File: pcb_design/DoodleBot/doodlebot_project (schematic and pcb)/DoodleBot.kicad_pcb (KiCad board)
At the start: 2 copper layers, 82.9 x 56.1 mm, 45 parts, among them J1 Conn_01x04, J2 Conn_01x04, J3 USB_B_Micro, J4 BUZZER_HEADERS, J5 LED_HEADERS, J6 MARKER_HEADERS, J7 ERASER_HEADERS, U1 ESP32-S3-WROOM-1

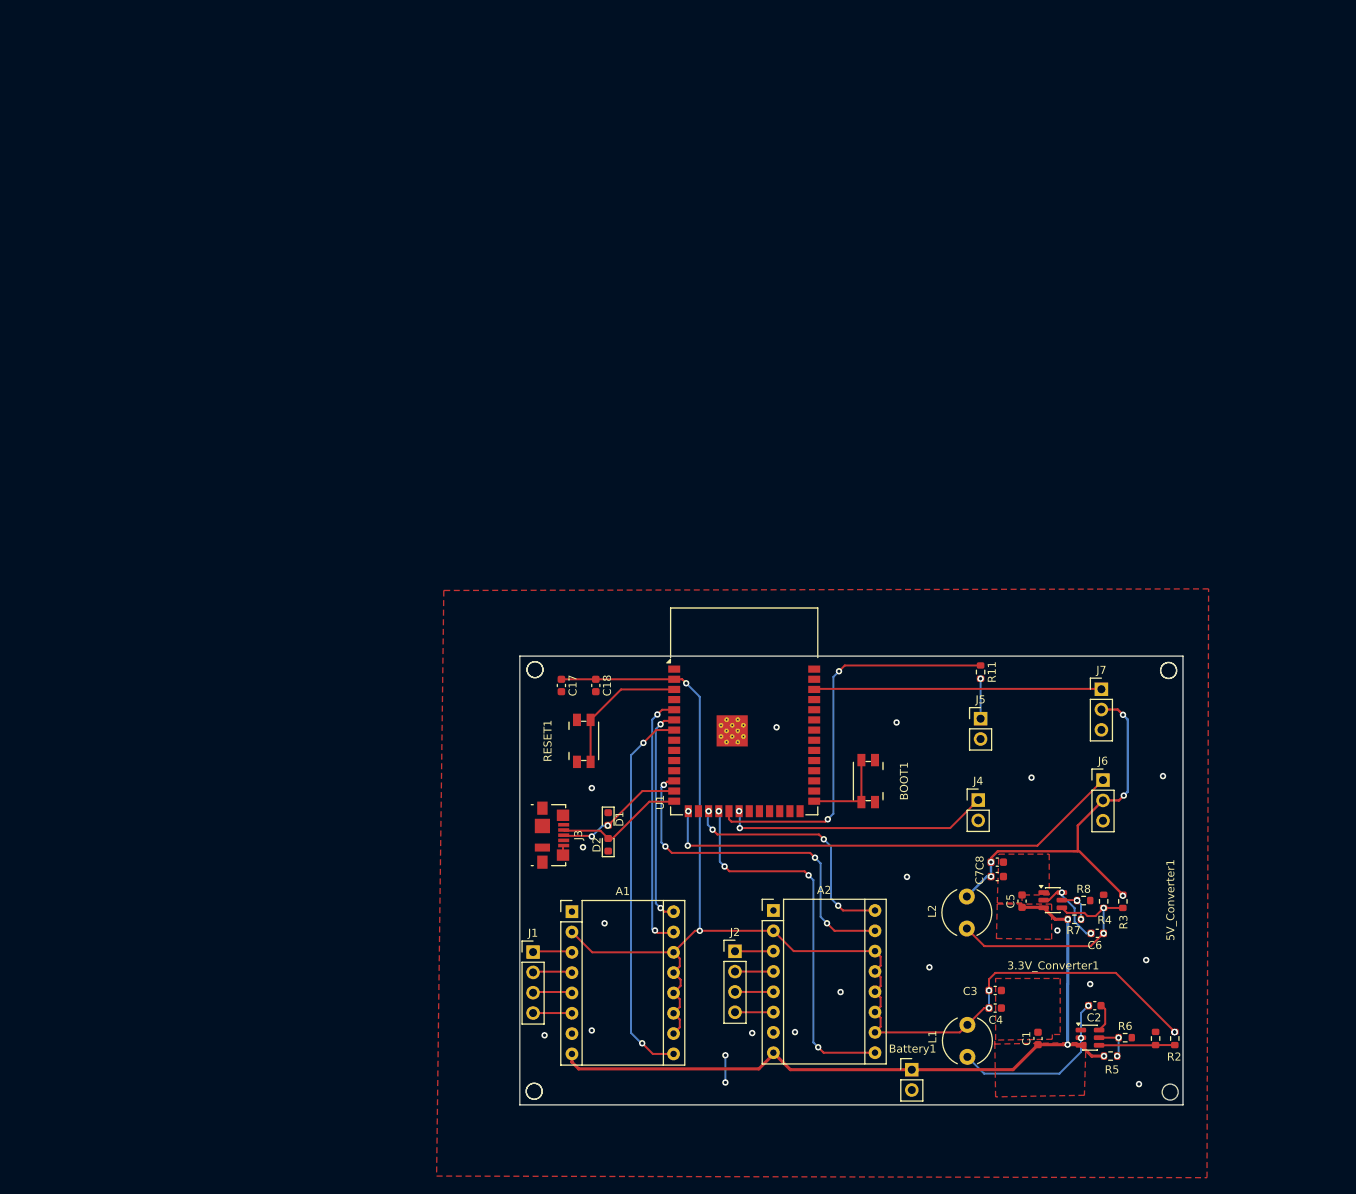
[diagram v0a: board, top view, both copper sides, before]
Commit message: Reorganized project structure
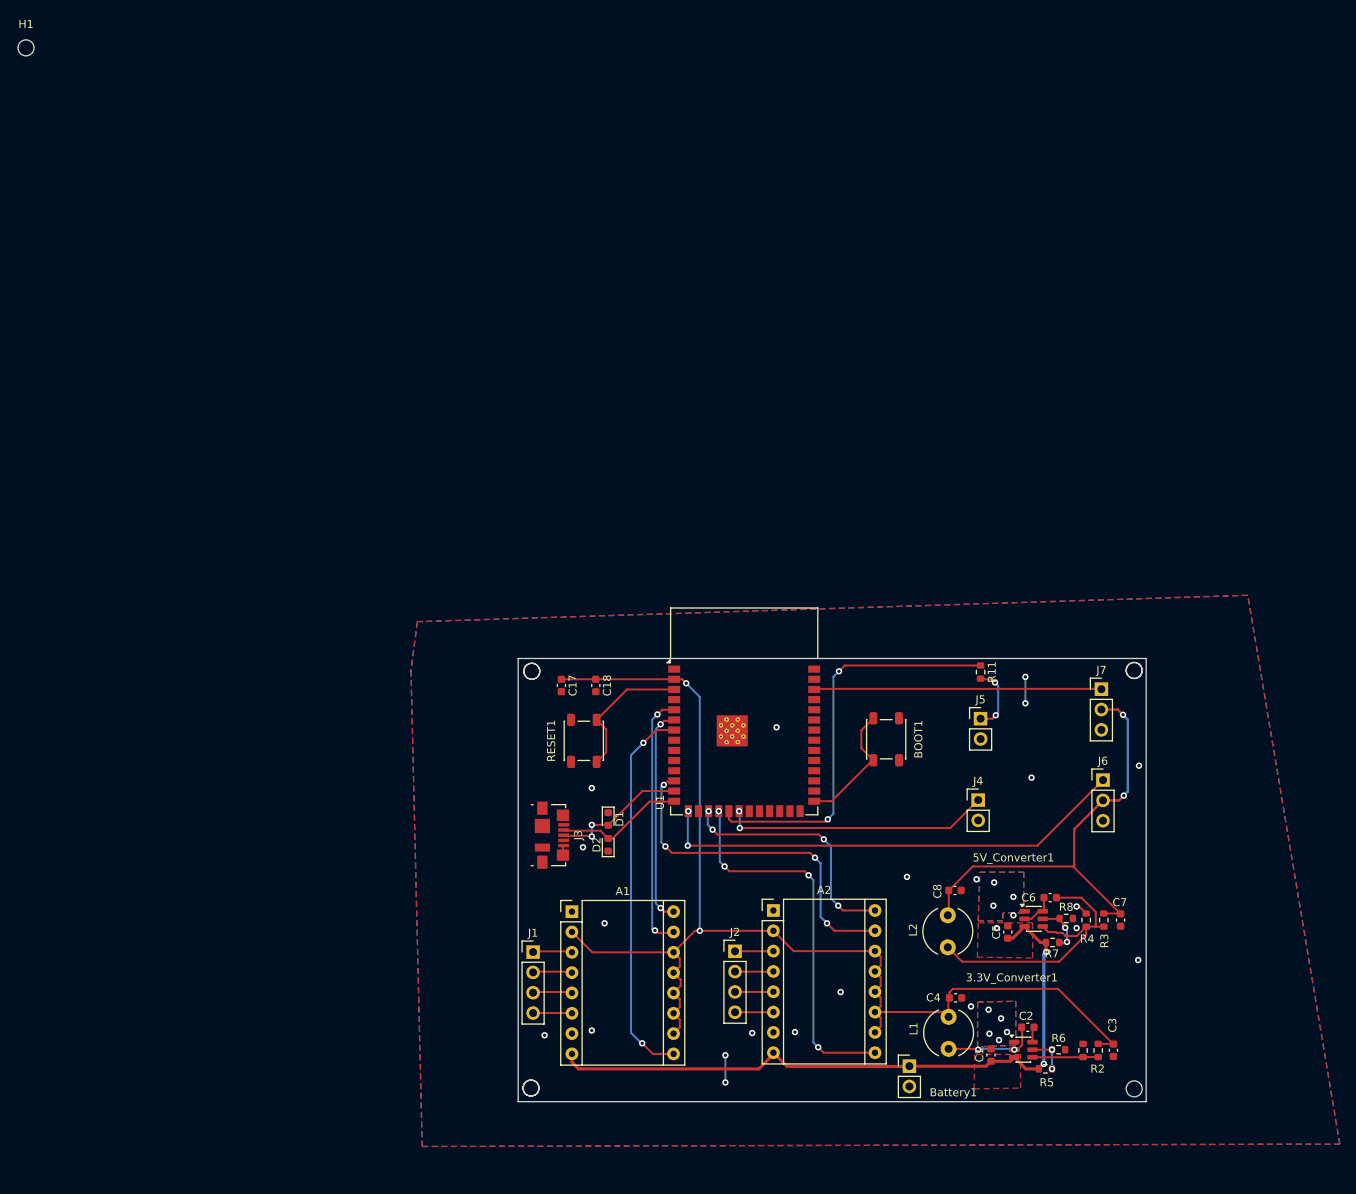
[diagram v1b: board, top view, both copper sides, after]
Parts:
- added H1: MountingHole, MountingHole:MountingHole_2mm, F.Cu at (2.27, 2.27)
- BOOT1, RESET1: footprint Button_Switch_SMD:Panasonic_EVQPUJ_EVQPUA -> Button_Switch_SMD:SW_SPST_PTS647_Sx38
- moved C3 16.6 mm to (138.2, 127.6), turned to 90 degrees
- moved C7 16.4 mm to (139.1, 111.3), turned to 90 degrees
- moved R2 9.69 mm to (136.3, 127.6)
- moved R1 9.20 mm to (134.4, 127.6)
- moved C2 8.80 mm to (127.5, 124.7)
- moved R6 8.46 mm to (131.3, 127.5)
- moved 3.3V_Converter1 8.46 mm to (127.0, 127.5)
- moved R5 8.31 mm to (129.7, 129.9)
- moved C6 7.38 mm to (130.3, 108.5)
- moved C8 6.36 mm to (118.4, 107.6)
- moved C1 6.23 mm to (122.9, 128.2)
- moved BOOT1 5.69 mm to (109.8, 88.7)
- moved C4 5.11 mm to (118.5, 121.0)
- moved ? 4.52 mm to (140.8, 132.4)
- moved ? 4.30 mm to (140.8, 80.1)
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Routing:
- net Net-(3.3V_Converter1-SW): track 22.4 -> 11.8 mm
- net +12V: track 93.8 -> 84.9 mm, vias 3 -> 2
- net +3V3: track 159.6 -> 152.0 mm, vias 6 -> 2
- net +5V: track 50.4 -> 56.7 mm, vias 5 -> 2
- net Net-(5V_Converter1-FB): track 30.5 -> 36.8 mm, vias 2 -> 0
- net Net-(5V_Converter1-BOOT): track 9.72 -> 4.52 mm, vias 2 -> 0
- net GND: track 5.01 -> 9.87 mm, vias 20 -> 31
- net Net-(U1-IO0): track 11.2 -> 16.0 mm
- net Net-(J5-Pin_1): track 5.00 -> 8.46 mm, vias 1 -> 2
- net Net-(5V_Converter1-EN): track 4.57 -> 6.97 mm, vias 3 -> 2
- net Net-(3.3V_Converter1-BOOT): track 3.64 -> 1.93 mm
- net Net-(3.3V_Converter1-FB): track 9.53 -> 8.22 mm
- net Net-(D1-A2): track 16.2 -> 17.1 mm
- added copper zone on B.Cu, net GND
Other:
- board size 82.9 x 56.1 mm -> 78.5 x 55.4 mm

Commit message: Added wider 12V traces from 0.39mm to 0.45mm
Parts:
- removed H1: MountingHole, MountingHole:MountingHole_2mm
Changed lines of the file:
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@@
 			(drillshape 0)
 			(scaleselection 1)
-			(outputdirectory "./")
+			(outputdirectory "doodlebot_gerber/")
 		)
 	)
@@
 		(embedded_fonts no)
 	)
-	(footprint "MountingHole:MountingHole_2mm"
-		(layer "F.Cu")
-		(at 2.275 2.275)
-		(descr "Mounting Hole 2mm, no annular, generated by kicad-footprint-generator mountinghole.py")
-		(tags "mountinghole")
-		(property "Reference" "H1"
-			(at 0 -2.95 0)
-			(layer "F.SilkS")
-			(effects
-				(font
-					(size 1 1)
-					(thickness 0.15)
-				)
-			)
-		)
-		(property "Value" "MountingHole"
-			(at 0 2.95 0)
-			(layer "F.Fab")
-			(effects
-				(font
-					(size 1 1)
-					(thickness 0.15)
-				)
-			)
-		)
-		(property "Datasheet" "~"
-			(at 0 0 0)
-			(layer "F.Fab")
-			(hide yes)
-			(effects
-				(font
-					(size 1.27 1.27)
-					(thickness 0.15)
-				)
-			)
-		)
-		(property "Description" "Mounting Hole without connection"
-			(at 0 0 0)
-			(layer "F.Fab")
-			(hide yes)
-			(effects
-				(font
-					(size 1.27 1.27)
-					(thickness 0.15)
-				)
-			)
-		)
-		(property ki_fp_filters "MountingHole*")
-		(sheetname "/")
-		(sheetfile "DoodleBot.kicad_sch")
-		(attr exclude_from_pos_files exclude_from_bom)
-		(fp_circle
-			(center 0 0)
-			(end 2 0)
-			(stroke
-				(width 0.15)
-				(type solid)
-			)
-			(fill no)
-			(layer "Cmts.User")
-		)
-		(fp_circle
-			(center 0 0)
-			(end 2.25 0)
-			(stroke
-				(width 0.05)
-				(type solid)
-			)
-			(fill no)
-			(layer "F.CrtYd")
-		)
-		(fp_text user "${REFERENCE}"
-			(at 0 0 0)
-			(layer "F.Fab")
-			(effects
-				(font
-					(size 1 1)
-					(thickness 0.15)
-				)
-			)
-		)
-		(pad "" np_thru_hole circle
-			(at 0 0)
-			(size 2 2)
-			(drill 2)
-			(layers "*.Cu" "*.Mask")
-		)
-		(embedded_fonts no)
-	)
 	(footprint ""
 		(layer "F.Cu")
@@
 		(start 125.3125 128.95)
 		(end 125.8125 128.45)
-		(width 0.39)
+		(width 0.45)
 		(layer "F.Cu")
 		(net 5)
@@
 		(start 127.2625 129.9)
 		(end 125.8125 128.45)
-		(width 0.39)
+		(width 0.45)
 		(layer "F.Cu")
 		(net 5)
@@
 		(start 128.875 129.9)
 		(end 127.2625 129.9)
-		(width 0.39)
+		(width 0.45)
 		(layer "F.Cu")
 		(net 5)
@@
 	)
 	(segment
-		(start 95.7 128.08)
-		(end 93.88 129.9)
-		(width 0.39)
-		(layer "F.Cu")
-		(net 5)
-	)
-	(segment
 		(start 129.775 114.1)
 		(end 129.775 115.275)
-		(width 0.39)
+		(width 0.45)
 		(layer "F.Cu")
 		(net 5)
 	)
 	(segment
-		(start 93.88 129.9)
-		(end 71.36 129.9)
+		(start 112.66 129.6)
+		(end 112.7 129.56)
 		(width 0.39)
 		(layer "F.Cu")
@@
 	)
 	(segment
-		(start 112.66 129.6)
-		(end 112.7 129.56)
-		(width 0.39)
+		(start 71.06 129.6)
+		(end 70.52 129.06)
+		(width 0.45)
 		(layer "F.Cu")
 		(net 5)
@@
 		(start 122.9 128.95)
 		(end 125.3125 128.95)
-		(width 0.39)
+		(width 0.45)
 		(layer "F.Cu")
 		(net 5)
@@
 		(start 112.7 129.56)
 		(end 122.29 129.56)
-		(width 0.39)
+		(width 0.45)
 		(layer "F.Cu")
 		(net 5)
@@
 		(start 129.5 129.275)
 		(end 128.875 129.9)
-		(width 0.39)
+		(width 0.45)
 		(layer "F.Cu")
 		(net 5)
@@
 		(start 97.42 129.6)
 		(end 112.66 129.6)
-		(width 0.39)
+		(width 0.45)
 		(layer "F.Cu")
 		(net 5)
@@
 	)
 	(segment
-		(start 70.52 129.06)
-		(end 70.52 128.03)
-		(width 0.39)
-		(layer "F.Cu")
-		(net 5)
-	)
-	(segment
 		(start 125.8125 128.45)
 		(end 125.75 128.45)
@@
 		(start 129.1 114.1)
 		(end 127.1 112.1)
-		(width 0.39)
+		(width 0.45)
+		(layer "F.Cu")
+		(net 5)
+	)
+	(segment
+		(start 95.7 128.08)
+		(end 94.18 129.6)
+		(width 0.45)
 		(layer "F.Cu")
 		(net 5)
@@
 		(start 95.7 127.88)
 		(end 97.42 129.6)
-		(width 0.39)
+		(width 0.45)
+		(layer "F.Cu")
+		(net 5)
+	)
+	(segment
+		(start 70.52 129.06)
+		(end 70.52 128.03)
+		(width 0.45)
 		(layer "F.Cu")
 		(net 5)
@@
 		(start 129.775 114.1)
 		(end 129.1 114.1)
-		(width 0.39)
+		(width 0.45)
 		(layer "F.Cu")
 		(net 5)
@@
 		(start 125.625 113.575)
 		(end 127.1 112.1)
-		(width 0.39)
+		(width 0.45)
 		(layer "F.Cu")
 		(net 5)
@@
 	)
 	(segment
-		(start 122.29 129.56)
-		(end 122.9 128.95)
-		(width 0.39)
+		(start 94.18 129.6)
+		(end 71.06 129.6)
+		(width 0.45)
 		(layer "F.Cu")
 		(net 5)
 	)
 	(segment
-		(start 71.36 129.9)
-		(end 70.52 129.06)
-		(width 0.39)
+		(start 122.29 129.56)
+		(end 122.9 128.95)
+		(width 0.45)
 		(layer "F.Cu")
 		(net 5)
@@
 		(start 129.5 115.6)
 		(end 129.5 129.275)
-		(width 0.39)
+		(width 0.45)
 		(layer "B.Cu")
 		(net 5)
@@
 	)
 	(segment
-		(start 131.099582 112.899)
-		(end 131.848418 112.899)
-		(width 0.25)
-		(layer "F.Cu")
-		(net 18)
-	)
-	(segment
-		(start 130.199418 112.8)
-		(end 131.000582 112.8)
+		(start 129.375 112.1)
+		(end 130.074 112.799)
 		(width 0.25)
 		(layer "F.Cu")
@@
 	)
 	(segment
-		(start 130.074 112.799)
-		(end 130.198418 112.799)
-		(width 0.25)
-		(layer "F.Cu")
-		(net 18)
-	)
-	(segment
 		(start 136 110.3)
 		(end 136 112.125)
@@
 	)
 	(segment
-		(start 132.151 113.201582)
-		(end 132.151 113.3)
-		(width 0.25)
-		(layer "F.Cu")
-		(net 18)
-	)
-	(segment
 		(start 131.4 116.5)
 		(end 134.8 113.1)
@@
 	)
 	(segment
-		(start 131.000582 112.8)
-		(end 131.099582 112.899)
+		(start 134.2 108.5)
+		(end 136 110.3)
 		(width 0.25)
 		(layer "F.Cu")
@@
 	)
 	(segment
-		(start 134.2 108.5)
-		(end 136 110.3)
+		(start 130.198418 112.799)
+		(end 130.199418 112.8)
 		(width 0.25)
 		(layer "F.Cu")
@@
 	)
 	(segment
-		(start 129.375 112.1)
-		(end 130.074 112.799)
+		(start 130.074 112.799)
+		(end 130.198418 112.799)
 		(width 0.25)
 		(layer "F.Cu")
@@
 	)
 	(segment
-		(start 133.625 113.3)
-		(end 134.8 112.125)
+		(start 117.5 114.7)
+		(end 119.3 116.5)
 		(width 0.25)
 		(layer "F.Cu")
@@
 	)
 	(segment
-		(start 117.5 114.7)
-		(end 119.3 116.5)
+		(start 130.199418 112.8)
+		(end 131.701765 112.8)
 		(width 0.25)
 		(layer "F.Cu")
@@
 	)
 	(segment
-		(start 134.575 112.15)
-		(end 134.6 112.125)
+		(start 132.201765 113.3)
+		(end 133.625 113.3)
 		(width 0.25)
 		(layer "F.Cu")
@@
 	)
 	(segment
-		(start 119.3 116.5)
-		(end 131.4 116.5)
+		(start 133.625 113.3)
+		(end 134.8 112.125)
 		(width 0.25)
 		(layer "F.Cu")
@@
 	)
 	(segment
-		(start 136.9 112.125)
-		(end 137 112.225)
+		(start 134.575 112.15)
+		(end 134.6 112.125)
 		(width 0.25)
 		(layer "F.Cu")
@@
 	)
 	(segment
-		(start 136 112.125)
-		(end 137 112.125)
+		(start 131.701765 112.8)
+		(end 132.201765 113.3)
 		(width 0.25)
 		(layer "F.Cu")
@@
 	)
 	(segment
-		(start 130.198418 112.799)
-		(end 130.199418 112.8)
+		(start 119.3 116.5)
+		(end 131.4 116.5)
 		(width 0.25)
 		(layer "F.Cu")
@@
 	)
 	(segment
-		(start 132.151 113.3)
-		(end 133.625 113.3)
+		(start 136.9 112.125)
+		(end 137 112.225)
 		(width 0.25)
 		(layer "F.Cu")
@@
 	)
 	(segment
-		(start 131.848418 112.899)
-		(end 132.151 113.201582)
+		(start 136 112.125)
+		(end 137 112.125)
 		(width 0.25)
 		(layer "F.Cu")
@@
 		(min_thickness 0.25)
 		(filled_areas_thickness no)
-		(fill yes
+		(fill
 			(thermal_gap 0.5)
 			(thermal_bridge_width 0.5)
@@
 		(polygon
 			(pts
-				(xy 50.4 80.1) (xy 51.8 139.6) (xy 166.5 139.3) (xy 155 70.7) (xy 51.2 74) (xy 50.4 80)
+				(xy 50.4 80.1) (xy 51.8 139.6) (xy 153.1 139.5) (xy 155 70.7) (xy 51.2 74) (xy 50.4 80)
 			)
 		)
